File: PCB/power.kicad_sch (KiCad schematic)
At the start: 46 parts, among them J1 USB_C_Receptacle_USB2.0_16P, J2 Battery, Q1 2N7002, Q2 2N7002, SW1 PWR, U10 BQ24074RGT, U13 TLV62569DBV, U8 USBLC6-2SC6, U9 TPS3424A11C13ADRLR

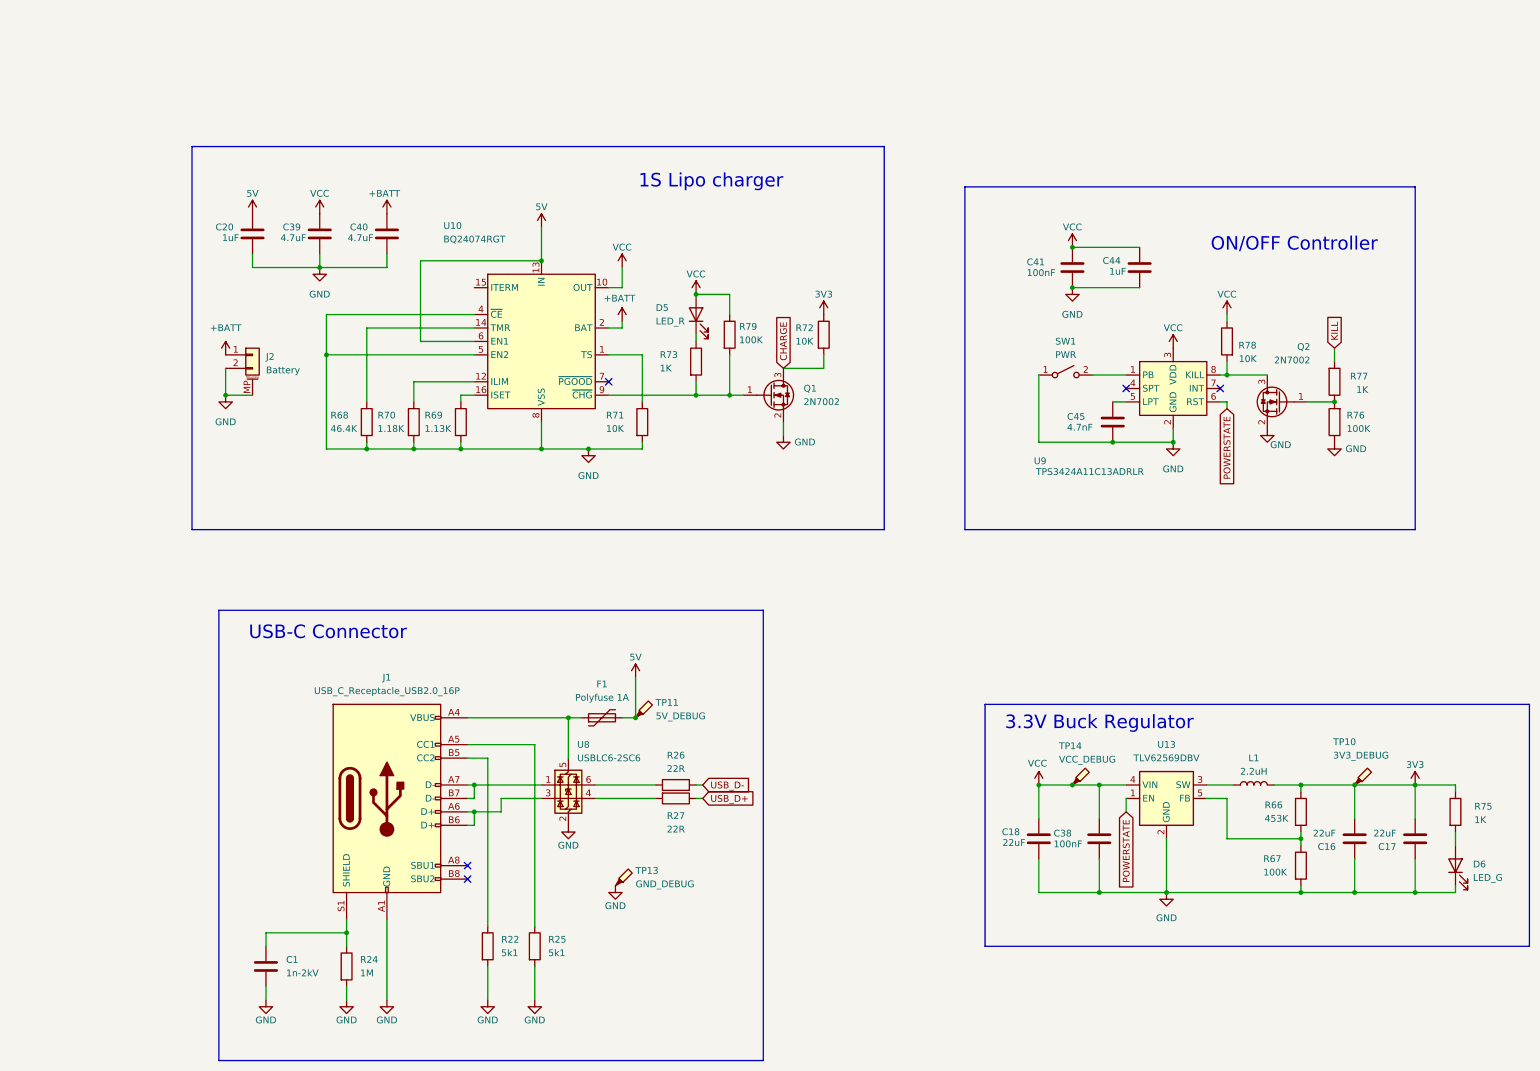
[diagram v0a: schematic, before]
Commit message: Review schematic
Fix errors / add improvements
Add gitignore file
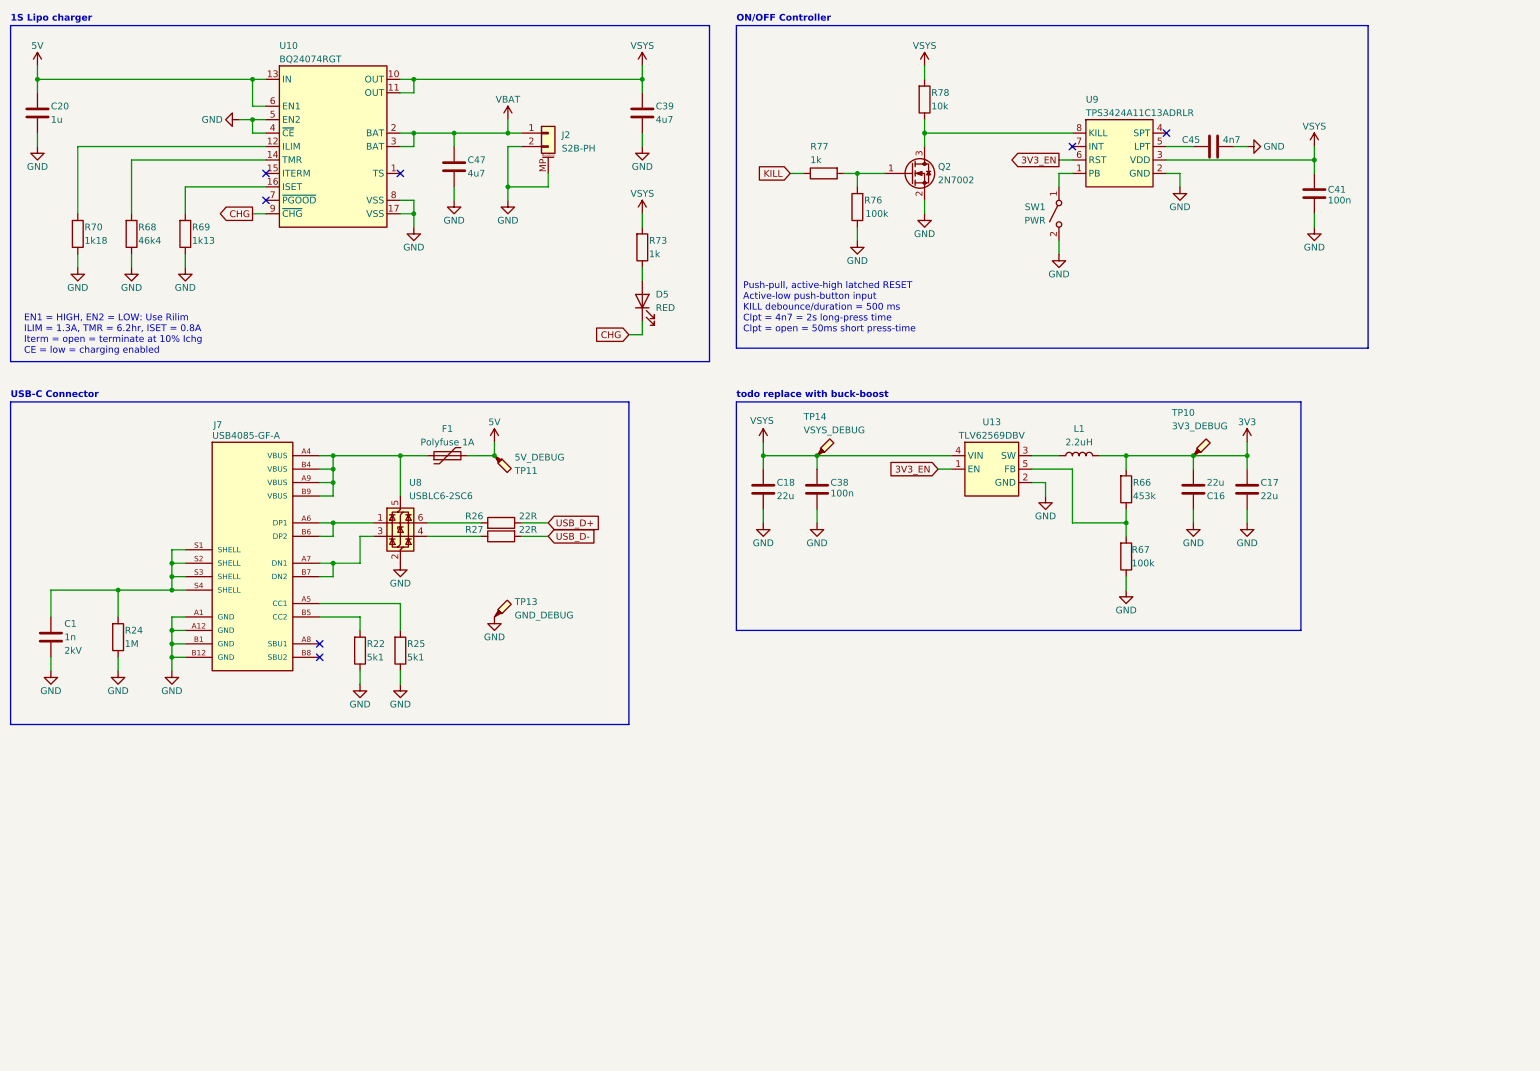
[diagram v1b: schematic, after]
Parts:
- removed C16, C17, C18: 22uF, Capacitor_SMD:C_0805_2012Metric, symbol Device:C
- removed C20, C44: 1uF, Capacitor_SMD:C_0805_2012Metric, symbol Device:C
- removed C40: 4.7uF, Capacitor_SMD:C_0805_2012Metric, symbol Device:C
- removed C45: 4.7nF, Capacitor_SMD:C_0603_1608Metric, symbol Device:C
- removed D5: LED_R, LED_SMD:LED_0603_1608Metric, symbol Device:LED
- removed D6: LED_G, LED_SMD:LED_0603_1608Metric, symbol Device:LED
- removed J1: USB_C_Receptacle_USB2.0_16P, Connector_USB:USB_C_Receptacle_Palconn_UTC16-G, symbol Connector:USB_C_Receptacle_USB2.0_16P
- removed Q1: 2N7002, Package_TO_SOT_SMD:SOT-23, symbol Transistor_FET:2N7002
- removed R68: 46.4K, Resistor_SMD:R_0603_1608Metric, symbol Device:R
- removed R69: 1.13K, Resistor_SMD:R_0603_1608Metric, symbol Device:R
- removed R70: 1.18K, Resistor_SMD:R_0603_1608Metric, symbol Device:R
- removed R71, R72, R78: 10K, Resistor_SMD:R_0603_1608Metric, symbol Device:R
- removed R73, R75: 1K, Resistor_SMD:R_0603_1608Metric, symbol Device:R
- removed R76, R79: 100K, Resistor_SMD:R_0603_1608Metric, symbol Device:R
- added C16, C17, C18: 22u, Capacitor_SMD:C_0805_2012Metric, symbol Zotec:C
- added C20: 1u, Capacitor_SMD:C_0805_2012Metric, symbol Zotec:C
- added C45: 4n7, Capacitor_SMD:C_0603_1608Metric, symbol Zotec:C
- added C47: 4u7, Capacitor_SMD:C_0805_2012Metric, symbol Zotec:C
- added D5: RED, LED_SMD:LED_0603_1608Metric, symbol Zotec:LED
- added J7: USB4085-GF-A, Connector_USB:USB_C_Receptacle_Palconn_UTC16-G, symbol Zotec:USB4085-GF-A
- added R68: 46k4, Resistor_SMD:R_0603_1608Metric, symbol Zotec:R
- added R69: 1k13, Resistor_SMD:R_0603_1608Metric, symbol Zotec:R
- added R70: 1k18, Resistor_SMD:R_0603_1608Metric, symbol Zotec:R
- added R73: 1k, Resistor_SMD:R_0603_1608Metric, symbol Zotec:R
- added R76: 100k, Resistor_SMD:R_0603_1608Metric, symbol Zotec:R
- added R78: 10k, Resistor_SMD:R_0603_1608Metric, symbol Zotec:R
- C1: value 1n-2kV -> 1n; symbol Device:C -> Zotec:C; Voltage (none) -> 2kV
- C38, C41: value 100nF -> 100n; symbol Device:C -> Zotec:C
- C39: value 4.7uF -> 4u7; symbol Device:C -> Zotec:C
- J2: value Battery -> S2B-PH
- R22, R24, R25, R26, R27: symbol Device:R -> Zotec:R
- R66: value 453K -> 453k; symbol Device:R -> Zotec:R
- R67: value 100K -> 100k; symbol Device:R -> Zotec:R
- R77: value 1K -> 1k; symbol Device:R -> Zotec:R
- TP14: value VCC_DEBUG -> VSYS_DEBUG
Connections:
- net 3V3: now also C16.1, C17.1
- net 5V: now also C20.1
- net GND: now also C39.2, SW1.2 (B), C16.2, C17.2, C18.2, C20.2, C45.2, C47.2, J7.A1 (GND), J7.A12 (GND), J7.B1 (GND), J7.B12 (GND), R68.2, R69.2, R70.2, R76.2; no longer C39.1, SW1.1 (A)
- net USB_D+: now also R26.2; no longer R27.1
- net USB_D-: now also R27.1; no longer R26.2
- net at Q2.1 (G), R77.1: now also R76.1
- net at Q2.3 (D), U9.8 (KILL): now also R78.2
- net at U9.1 (PB): now also SW1.1 (A); no longer SW1.2 (B)
- net at U9.5 (LPT): now also C45.1
- net at F1.1, U8.5 (VBUS): now also J7.A4 (VBUS), J7.A9 (VBUS), J7.B4 (VBUS), J7.B9 (VBUS)
- net at R25.1: now also J7.A5 (CC1)
- net at U8.3 (I/O2): now also J7.A7 (DN1), J7.B7 (DN2)
- net at U8.1 (I/O1): now also J7.A6 (DP1), J7.B6 (DP2)
- net at R22.1: now also J7.B5 (CC2)
- net at C1.1, R24.1: now also J7.S1 (SHELL), J7.S2 (SHELL), J7.S3 (SHELL), J7.S4 (SHELL)
- net at U10.12 (ILIM): now also R70.1
- net at U10.16 (ISET): now also R69.1
- net at U10.14 (TMR): now also R68.1
- net CHG: now reaches U10.9 (~{CHG})
- net CHG: now also D5.K
- net +BATT renamed VBAT
- net VBAT: now also C47.1
- net POWERSTATE renamed 3V3_EN
- net VCC renamed VSYS
- net VSYS: now also C39.1, C18.1, R73.1, R78.1; no longer C39.2
- new net: D5.A, R73.2
- no-connect marks 5 -> 7
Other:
- note added: "EN1 = HIGH, EN2 = LOW: Use Rilim ILIM = 1.3A, TMR = 6.2hr, ISET = 0.8A Iterm = open = terminate at 10% Ichg CE = low = charging enabled"
- note added: "Push-pull, active-high latched RESET Active-low push-button input KILL debounce/duration = 500 ms Clpt = 4n7 = 2s long-press time Clpt = open = 50ms short press-time"
- note added: "todo replace with buck-boost"
- note removed: "3.3V Buck Regulator"
- company: ProtoIoT -> ${Company_name}
- title: Stabielator -> ${Project_name}
- moved on the sheet: C1, C38, C39, C41, F1, J2, L1, Q2, R22, R24, R25, R26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

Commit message: Hopelijk definitief schema
Voornamelijk voeding opnieuw gemaakt;
Vervangen voor een buck boost systeem.
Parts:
- removed C16, C17, C18: 22u, Capacitor_SMD:C_0805_2012Metric, symbol Zotec:C
- removed C38: 100n, Capacitor_SMD:C_0603_1608Metric, symbol Zotec:C
- removed L1: 2.2uH, Inductor_SMD:L_1008_2520Metric, symbol Device:L
- removed TP10: 3V3_DEBUG, TestPoint:TestPoint_Pad_D1.0mm, symbol Connector:TestPoint_Probe
- removed TP14: VSYS_DEBUG, TestPoint:TestPoint_Pad_D1.0mm, symbol Connector:TestPoint_Probe
- removed U13: TLV62569DBV, Package_TO_SOT_SMD:SOT-23-5, symbol Regulator_Switching:TLV62569DBV
- added C48, C51, C52: 10u, Capacitor_SMD:C_1206_3216Metric, symbol Device:C
- added C50, C53: 100n, Capacitor_SMD:C_0603_1608Metric, symbol Zotec:C
- added L3: 2.2u, Inductor_SMD:L_Bourns-SRN4018, symbol Device:L
- added R74: 100R, Resistor_SMD:R_0603_1608Metric, symbol Zotec:R
- added R79: 10k, Resistor_SMD:R_0603_1608Metric, symbol Zotec:R
- added TP12: 3V3_DEBUG, TestPoint:TestPoint_Pad_D1.0mm, symbol Connector:TestPoint_Probe
- added TP15: VSYS_DEBUG, TestPoint:TestPoint_Pad_D1.0mm, symbol Connector:TestPoint_Probe
- added U40: TPS63001, Package_SON:Texas_DRC0010J_ThermalVias, symbol Regulator_Switching:TPS63001
- C1: Digikey (none) -> 399-C1206C102KGRACTUCT-ND; LCSC C9196 -> (none)
- C20: Digikey (none) -> 490-1691-1-ND; LCSC C28323 -> (none)
- C39: Digikey (none) -> 490-14466-1-ND; LCSC C28323 -> (none)
- C40: renamed from C47; Digikey (none) -> 490-14466-1-ND; LCSC C28323 -> (none)
- C41: Digikey (none) -> 399-C0603C104K5RACTUCT-ND
- C45: Digikey (none) -> 445-173690-1-ND
- D5: Digikey (none) -> 732-12015-1-ND
- F1: Digikey (none) -> 5923-0ZCK0100FF2ECT-ND; LCSC C910822 -> (none)
- J1: renamed from J7; value USB4085-GF-A -> USB4105-GF-A; Digikey (none) -> 2073-USB4105-GF-ACT-ND
- J2: Digikey (none) -> 455-S2B-PH-SM4-TBCT-ND
- R22, R25: Digikey (none) -> YAG3621CT-ND; LCSC C23186 -> (none)
- R24: Digikey (none) -> 311-1.00MHRCT-ND; LCSC C22935 -> (none)
- R26, R27: Digikey (none) -> YAG3581CT-ND; LCSC C23186 -> (none)
- R66: value 453k -> 300k 0.1%; Digikey 311-10.0KHRCT-ND -> YAG1627CT-ND
- R67: value 100k -> 100k 0.1%; Digikey 311-10.0KHRCT-ND -> YAG1235CT-ND
- R68: Digikey 311-10.0KHRCT-ND -> 311-46.4KHRCT-ND
- R69: Digikey 311-10.0KHRCT-ND -> 311-1.13KHRCT-ND
- R70: Digikey 311-10.0KHRCT-ND -> 311-1.18KHRCT-ND
- R73, R77: Digikey 311-10.0KHRCT-ND -> 311-1.00KHRCT-ND
- R76: Digikey 311-10.0KHRCT-ND -> 311-100KHRCT-ND
- SW1: Digikey (none) -> 4809-SKRTLAE010CT-ND
- TP11, TP13: Digikey (none) -> nvt
- U8: Digikey (none) -> 5399-USBLC6-2SC6CT-ND; LCSC C2687116 -> (none)
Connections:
- net 3V3: now also C51.1, C52.1, TP12.1, U40.1 (VOUT), U40.10 (FB); no longer R66.1
- net 3V3_EN: now also U40.6 (EN)
- net GND: now also C48.2, C50.2, C51.2, C52.2, C53.2, R79.2, U40.11 (PGND), U40.3 (PGND), U40.7 (PS/SYNC), U40.9 (GND)
- net VBAT: now also R66.1
- net VSYS: now also C48.1, R74.1, TP15.1, U40.5 (VIN)
- net BATTERY: now reaches R66.2, R67.1
- net BATTERY: now also C53.1
- net at U10.1 (TS): now also R79.1
- new net: L3.2, U40.2 (L2)
- new net: L3.1, U40.4 (L1)
- new net: C50.1, R74.2, U40.8 (VINA)
- no-connect marks 7 -> 6
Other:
- note added: "Battery measurement (might need load switch or removal of feature)"
- note added: "Buck Boost converter"
- note removed: "todo replace with buck-boost"
- moved on the sheet: C40, J2

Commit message: Edit BOM
Add manufacturer
Add partnumber
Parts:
- C1: Manufacturer (none) -> KEMET; Partnumber (none) -> C1206C102KGRACTU
- C20: Manufacturer (none) -> Murata Electronics; Partnumber (none) -> GRM21BR71C105KA01L
- C39, C40: Manufacturer (none) -> Murata Electronics; Partnumber (none) -> GRM21BR71C475KE51L
- C41, C50, C53: Manufacturer (none) -> KEMET; Partnumber (none) -> C0603C104K5RACTU
- C45: Manufacturer (none) -> TDK; Partnumber (none) -> C1608X7R1H472K080AE
- C48, C51, C52: Manufacturer (none) -> TDK; Partnumber (none) -> CGA5L1X7R1C106K160AC
- D5: Manufacturer (none) -> Würth Elektronik; Partnumber (none) -> 150060RS55040
- F1: Manufacturer (none) -> Bel Fuse Inc.; Partnumber (none) -> 0ZCK0100FF2E
- J1: Manufacturer (none) -> GCT; Partnumber (none) -> USB4105-GF-A
- J2: Manufacturer (none) -> JST Sales America Inc.; Partnumber (none) -> S2B-PH-SM4-TB
- L3: Manufacturer (none) -> Bourns Inc.; Partnumber (none) -> SRN4018-2R2M
- Q2: Manufacturer (none) -> onsemi; Partnumber (none) -> 2N7002
- R22, R25: Manufacturer (none) -> YAGEO; Partnumber (none) -> AC0603FR-075K1L
- R24: Manufacturer (none) -> YAGEO; Partnumber (none) -> RC0603FR-071ML
- R26, R27: Manufacturer (none) -> YAGEO; Partnumber (none) -> AC0603FR-0722RL
- R66: Manufacturer (none) -> YAGEO; Partnumber (none) -> RT0603BRD07300KL
- R67: Manufacturer (none) -> YAGEO; Partnumber (none) -> RT0603BRD07100KL
- R68: Manufacturer (none) -> YAGEO; Partnumber (none) -> RC0603FR-0746K4L
- R69: Manufacturer (none) -> YAGEO; Partnumber (none) -> RC0603FR-071K13L
- R70: Manufacturer (none) -> YAGEO; Partnumber (none) -> RC0603FR-071K18L
- R73, R77: Manufacturer (none) -> YAGEO; Partnumber (none) -> RC0603FR-071KL
- R74: Manufacturer (none) -> YAGEO; Partnumber (none) -> RC0603FR-07100RL
- R76: Manufacturer (none) -> YAGEO; Partnumber (none) -> RC0603FR-07100KL
- R78, R79: Manufacturer (none) -> YAGEO; Partnumber (none) -> RC0603FR-0710KL
- SW1: Manufacturer (none) -> Alps Alpine; Partnumber (none) -> SKRTLAE010
- U10: Manufacturer (none) -> Texas Instruments; Partnumber (none) -> BQ24074RGTR
- U40: Manufacturer (none) -> Texas Instruments; Partnumber (none) -> TPS63001DRCR
- U8: Manufacturer (none) -> Shenzhen Slkormicro Semicon Co., Ltd.; Partnumber (none) -> USBLC6-2SC6
- U9: Manufacturer (none) -> Texas Instruments; Partnumber (none) -> TPS3424A11C13ADRLR

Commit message: Reannotated schematic based on component placement
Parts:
- renumbered C53 to C10, C50 to C11, C20 to C12, C39 to C13, C48 to C14, C1 to C25, C45 to C27, C41 to C28, C51 to C7, C40 to C8, C52 to C9, D5 to D2, J2 to J1, J1 to J5, L3 to L1, Q2 to Q1, R67 to R1, R70 to R10, R26 to R15, R27 to R16, R68 to R17, R79 to R19, R66 to R2, R69 to R21, R25 to R24, R24 to R26, R22 to R28, R78 to R30, R76 to R31, R77 to R32, R74 to R4, R73 to R5, SW1 to SW2, TP15 to TP3, U8 to U10, U10 to U3, U40 to U4

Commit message: Finish concept layout and routing
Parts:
- removed D2: RED, LED_SMD:LED_0603_1608Metric, symbol Zotec:LED
- added D3: LED, LED_SMD:LED_0603_1608Metric, symbol Device:LED
- added TP14: EN_DEBUG, TestPoint:TestPoint_Pad_D1.0mm, symbol Connector:TestPoint_Probe
- added TP15: KILL_DEBUG, TestPoint:TestPoint_Pad_D1.0mm, symbol Connector:TestPoint_Probe
- added TP16: PSW_DEBUG, TestPoint:TestPoint_Pad_D1.0mm, symbol Connector:TestPoint_Probe
- added TP17: CHG_DEBUG, TestPoint:TestPoint_Pad_D1.0mm, symbol Connector:TestPoint_Probe
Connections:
- net 3V3_EN: now also TP14.1
- net CHG: now also D3.1 (K), TP17.1
- net KILL: now also TP15.1
- net USB_D+: now also R16.1; no longer R15.2
- net USB_D-: now also R15.2; no longer R16.1
- net at R5.2: now also D3.2 (A)
- net at SW2.1 (A), U9.1 (PB): now also TP16.1
- net at J5.A6 (DP1), J5.B6 (DP2): now also U10.3 (I/O2); no longer U10.1 (I/O1)
- net at J5.A7 (DN1), J5.B7 (DN2): now also U10.1 (I/O1); no longer U10.3 (I/O2)
- new net: C25.1, J5.SH (SHELL), R26.1
